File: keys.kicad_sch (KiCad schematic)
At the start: 4 parts

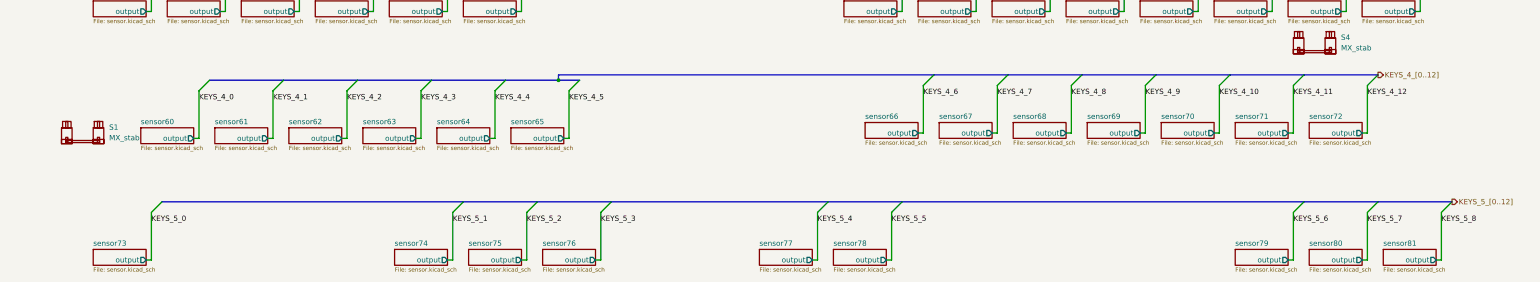
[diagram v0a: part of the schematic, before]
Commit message: Added Extra B and Started Multiplexer Layout
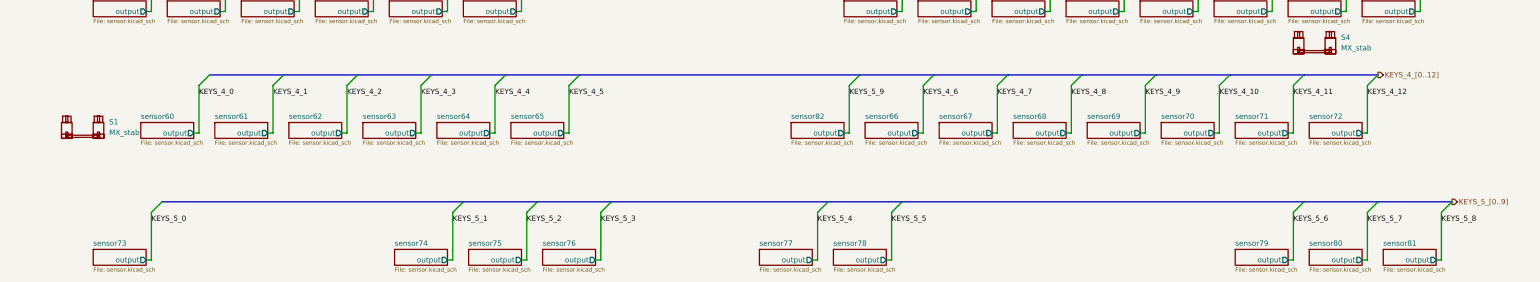
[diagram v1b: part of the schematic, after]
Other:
- added sheet sensor82 (sensor.kicad_sch)
- moved on the sheet: S1

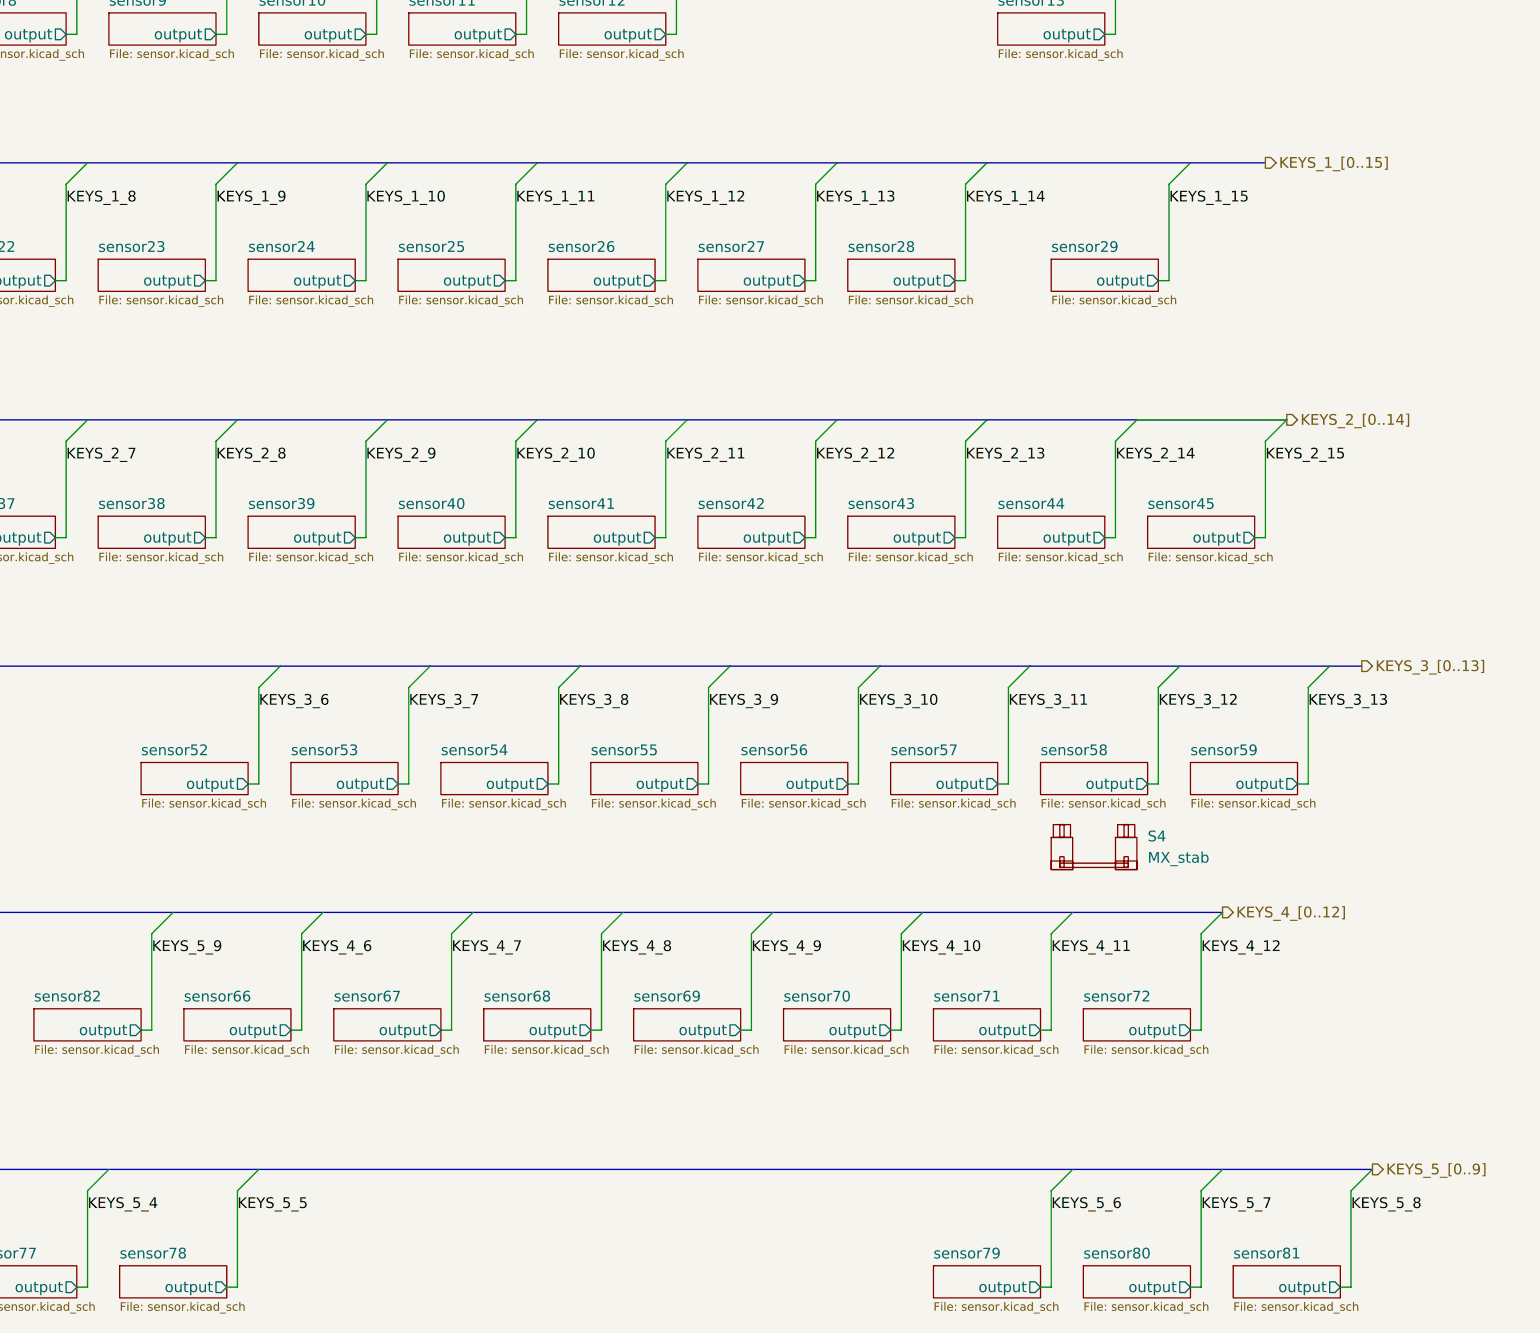
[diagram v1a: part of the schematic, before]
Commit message: Added All Keys to Multiplexers
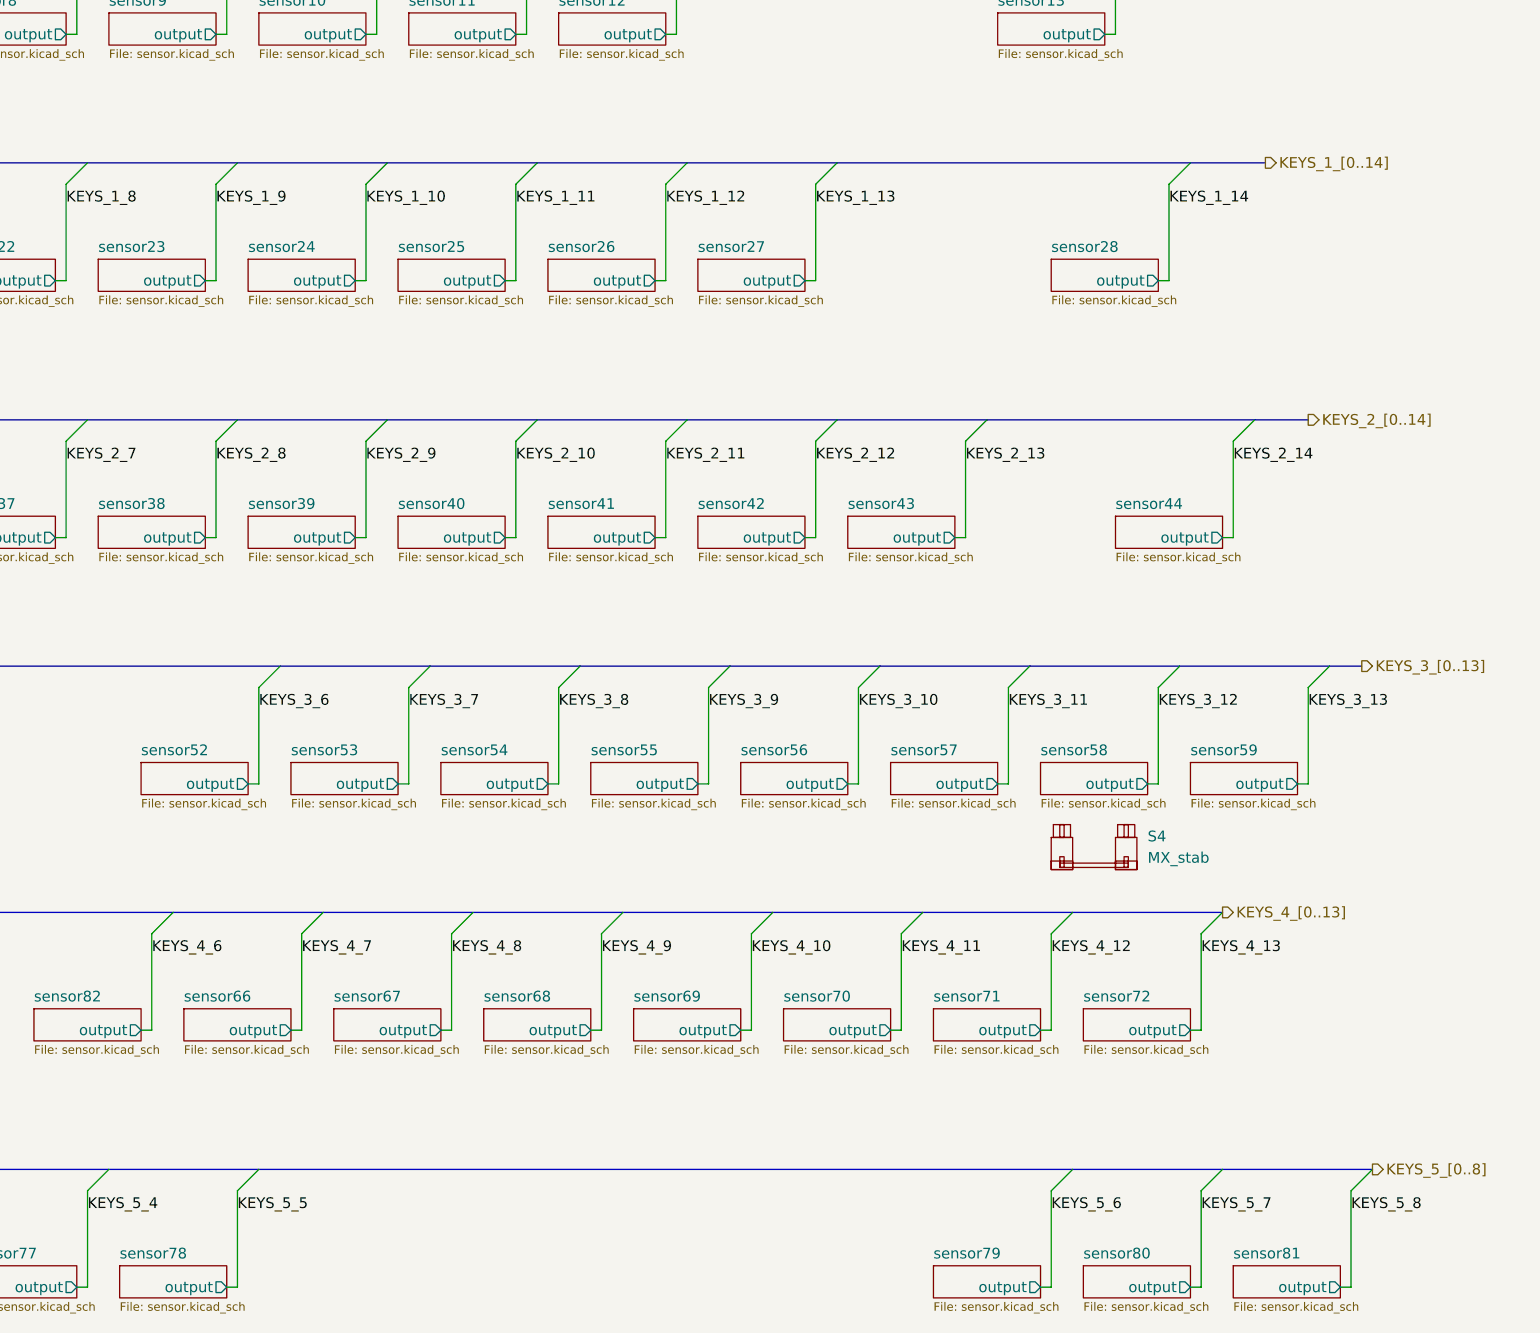
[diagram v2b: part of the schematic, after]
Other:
- removed sheet sensor29
- removed sheet sensor45

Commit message: Setup Base Layout
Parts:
- added S28: MX_stab, PCM_marbastlib-mx:STAB_MX_P_2u, symbol PCM_marbastlib-mx:MX_stab
- renumbered S4 to S57, S1 to S59, S2 to S75, S3 to S77
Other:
- removed sheet sensor81
- removed sheet sensor82
- added sheet sensor29 (sensor.kicad_sch)
- added sheet sensor45 (sensor.kicad_sch)

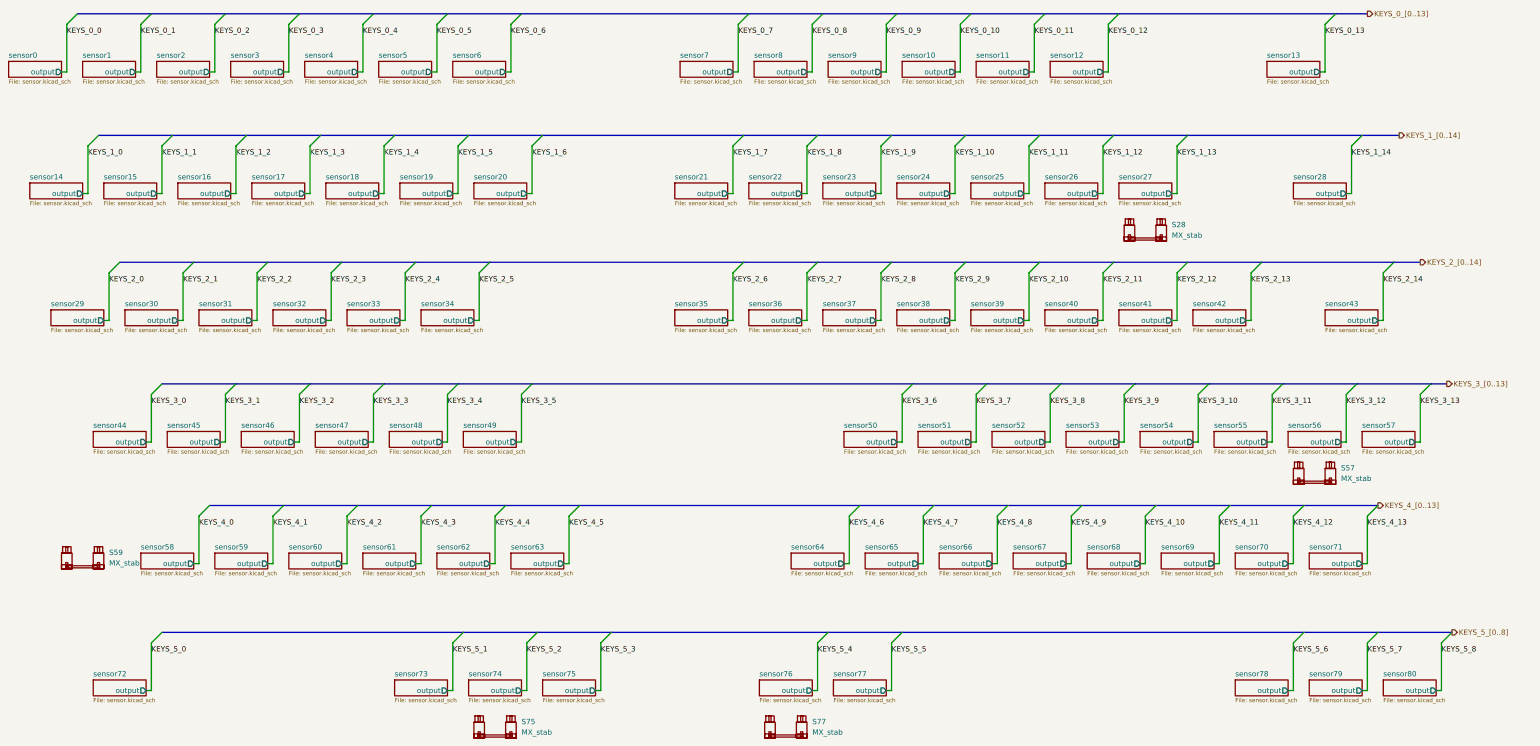
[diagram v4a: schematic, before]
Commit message: Routed a lot of the pcb, additionally fixed issues with wrong layout
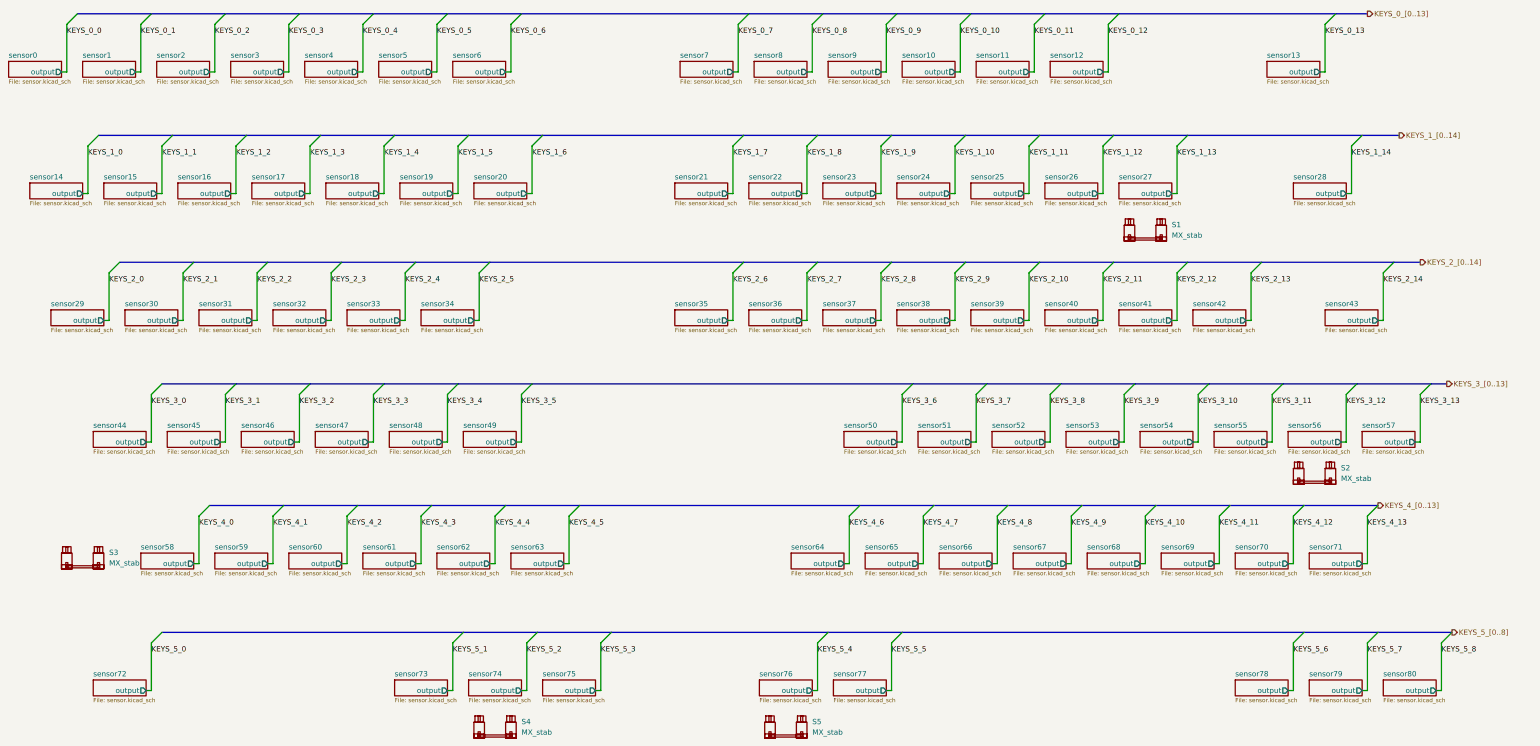
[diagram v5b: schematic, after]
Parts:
- renumbered S28 to S1, S57 to S2, S59 to S3, S75 to S4, S77 to S5
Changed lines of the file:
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@@
 		(dnp no)
 		(fields_autoplaced yes)
-		(property "Reference" "S77"
+		(property "Reference" "S5"
 			(at 237.49 195.453 0)
 			(effects
@@
 			(project "Erebus"
 				(path "/d88b0230-c6e0-4e9b-98a2-e29afd320bb6/a87a9230-372e-45a2-97eb-0c46b92f006f/d0b129e8-fd05-4742-a062-660bf68fb884"
-					(reference "S77")
+					(reference "S5")
 					(unit 1)
 				)
@@
 		(dnp no)
 		(fields_autoplaced yes)
-		(property "Reference" "S28"
+		(property "Reference" "S1"
 			(at 323.85 76.073 0)
 			(effects
@@
 			(project "Erebus"
 				(path "/d88b0230-c6e0-4e9b-98a2-e29afd320bb6/a87a9230-372e-45a2-97eb-0c46b92f006f/d0b129e8-fd05-4742-a062-660bf68fb884"
-					(reference "S28")
+					(reference "S1")
 					(unit 1)
 				)
@@
 		(dnp no)
 		(fields_autoplaced yes)
-		(property "Reference" "S57"
+		(property "Reference" "S2"
 			(at 364.49 134.493 0)
 			(effects
@@
 			(project "Erebus"
 				(path "/d88b0230-c6e0-4e9b-98a2-e29afd320bb6/a87a9230-372e-45a2-97eb-0c46b92f006f/d0b129e8-fd05-4742-a062-660bf68fb884"
-					(reference "S57")
+					(reference "S2")
 					(unit 1)
 				)
@@
 		(dnp no)
 		(fields_autoplaced yes)
-		(property "Reference" "S59"
+		(property "Reference" "S3"
 			(at 68.58 154.813 0)
 			(effects
@@
 			(project "Erebus"
 				(path "/d88b0230-c6e0-4e9b-98a2-e29afd320bb6/a87a9230-372e-45a2-97eb-0c46b92f006f/d0b129e8-fd05-4742-a062-660bf68fb884"
-					(reference "S59")
+					(reference "S3")
 					(unit 1)
 				)
@@
 		(dnp no)
 		(fields_autoplaced yes)
-		(property "Reference" "S75"
+		(property "Reference" "S4"
 			(at 167.64 195.453 0)
 			(effects
@@
 			(project "Erebus"
 				(path "/d88b0230-c6e0-4e9b-98a2-e29afd320bb6/a87a9230-372e-45a2-97eb-0c46b92f006f/d0b129e8-fd05-4742-a062-660bf68fb884"
-					(reference "S75")
-					(unit 1)
-				)
+					(reference "S4")
+					(unit 1)
+				)
